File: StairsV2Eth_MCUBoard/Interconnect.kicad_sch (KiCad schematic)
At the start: 3 parts, among them J14 Conn_01x18, J15 Conn_01x04

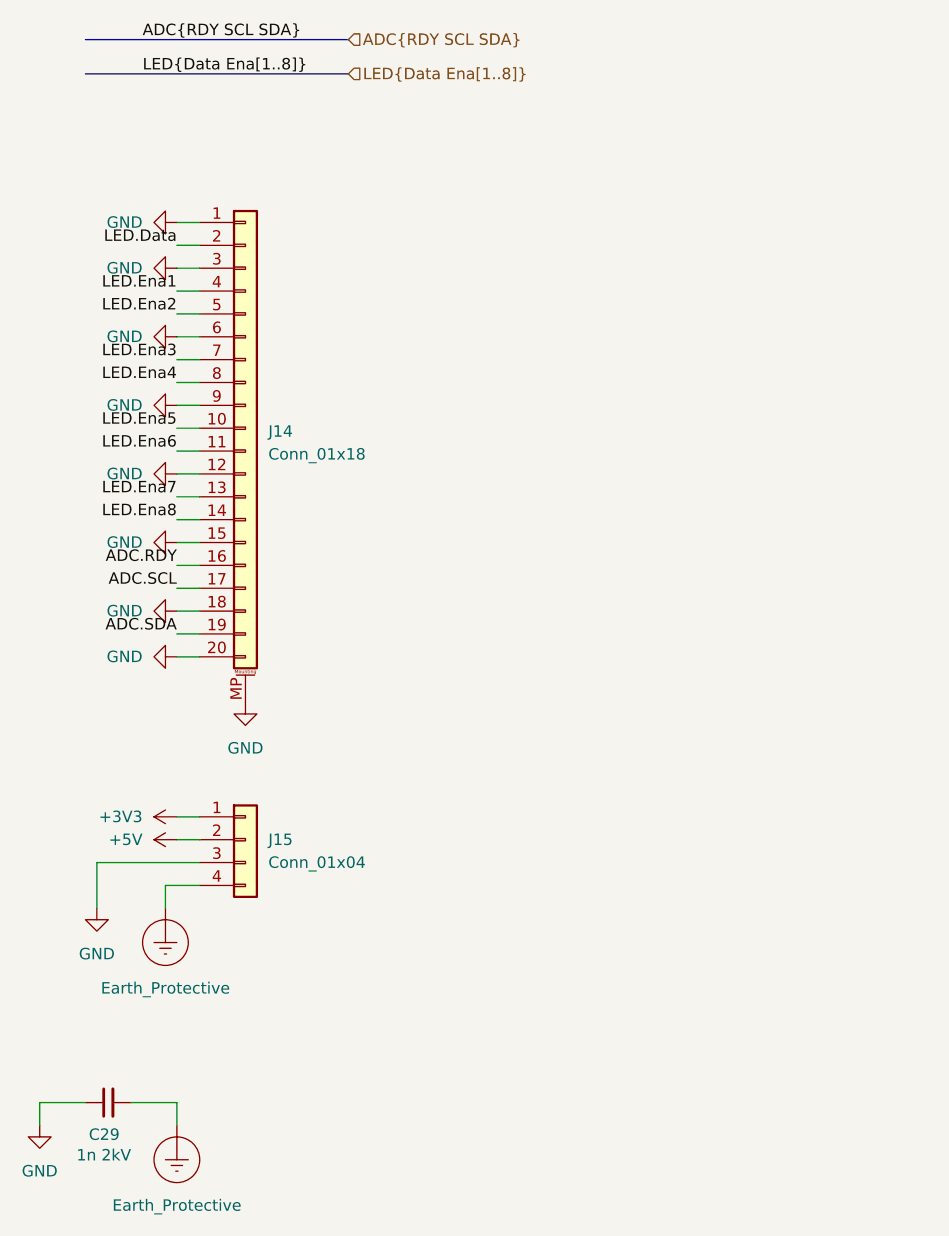
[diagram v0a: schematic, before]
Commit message: Ethernet on the MCU Board
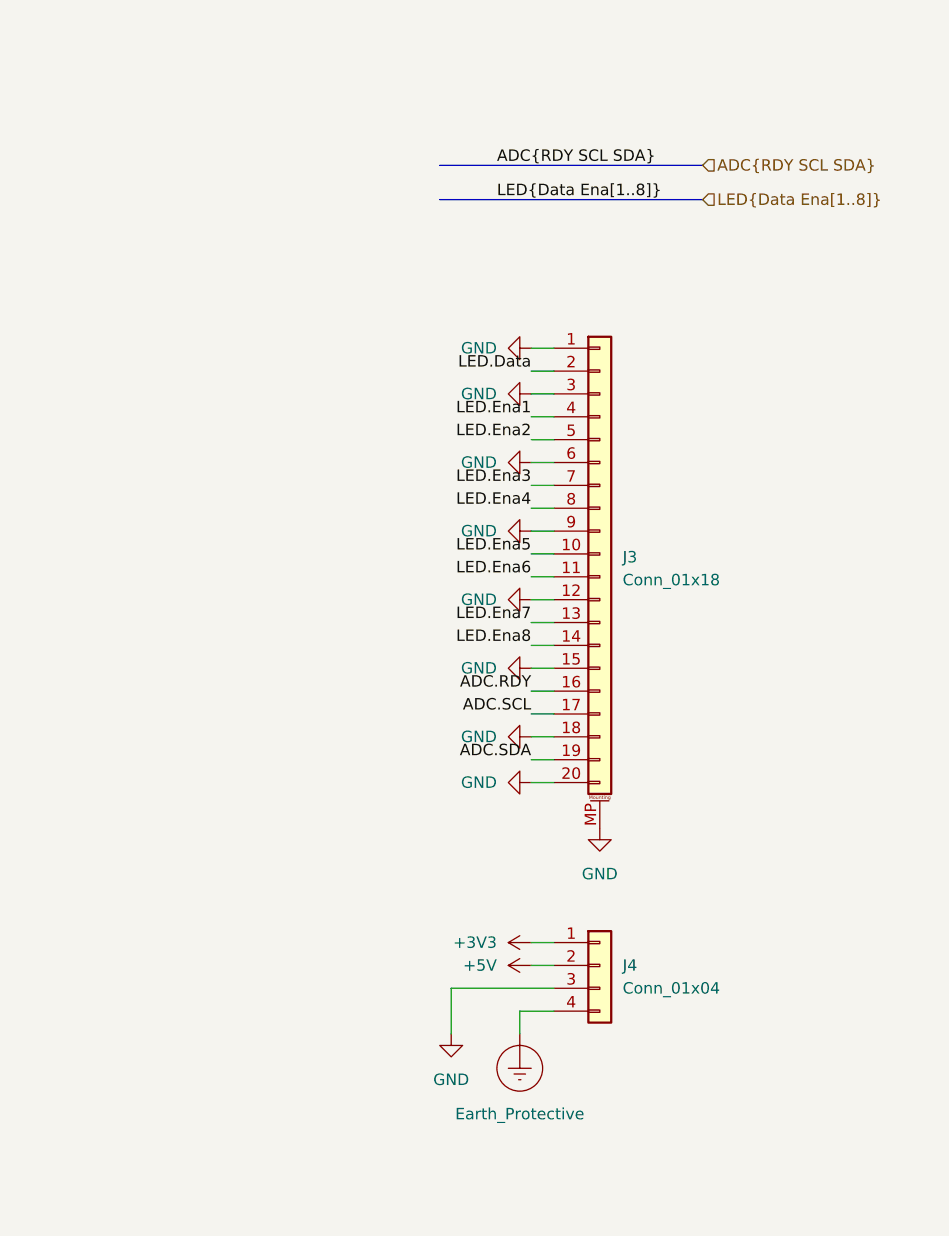
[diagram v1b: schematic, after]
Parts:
- removed C29: 1n 2kV, Capacitor_THT:C_Disc_D7.5mm_W2.5mm_P5.00mm, symbol Device:C_Small
- renumbered J14 to J3, J15 to J4
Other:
- moved on the sheet: J3, J4
